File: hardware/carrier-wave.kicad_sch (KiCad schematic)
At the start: 22 parts, among them J1 USB C 2.0, U1 STM32G0B1CBTx, U2 OPA695, U3 THS3491, U4 AD9834, U5 LM27762, U7 TS5A3159ADCK, U8 LM2990SX-12, U9 LM2940S-12

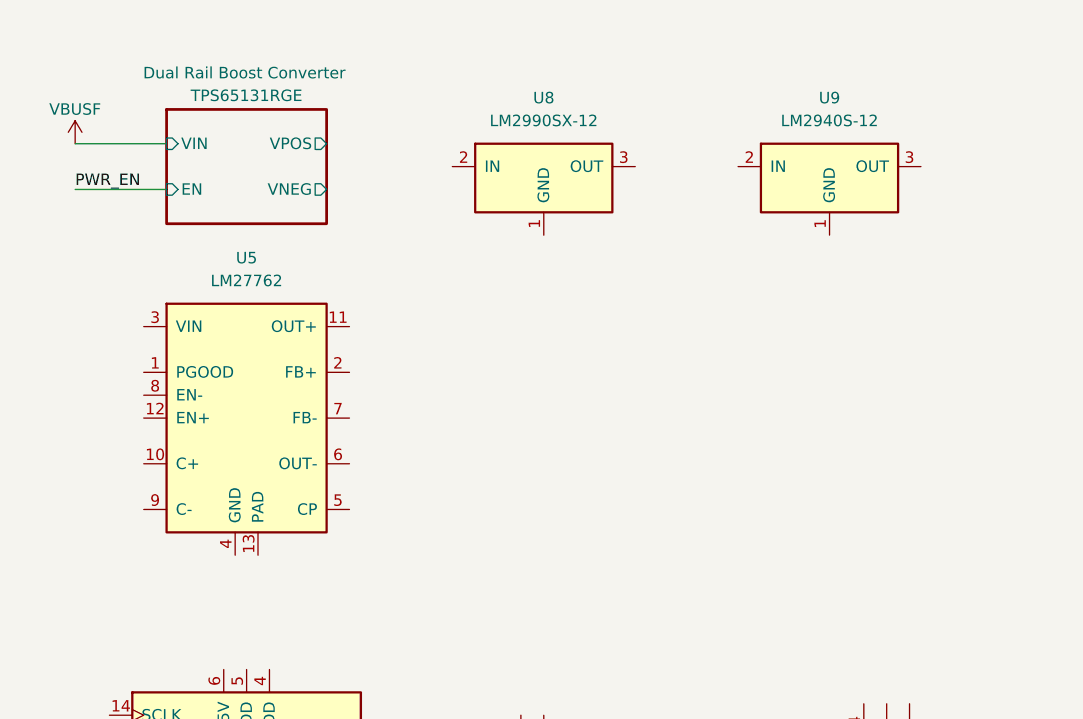
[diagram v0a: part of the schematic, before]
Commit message: Complete 12V rail supply
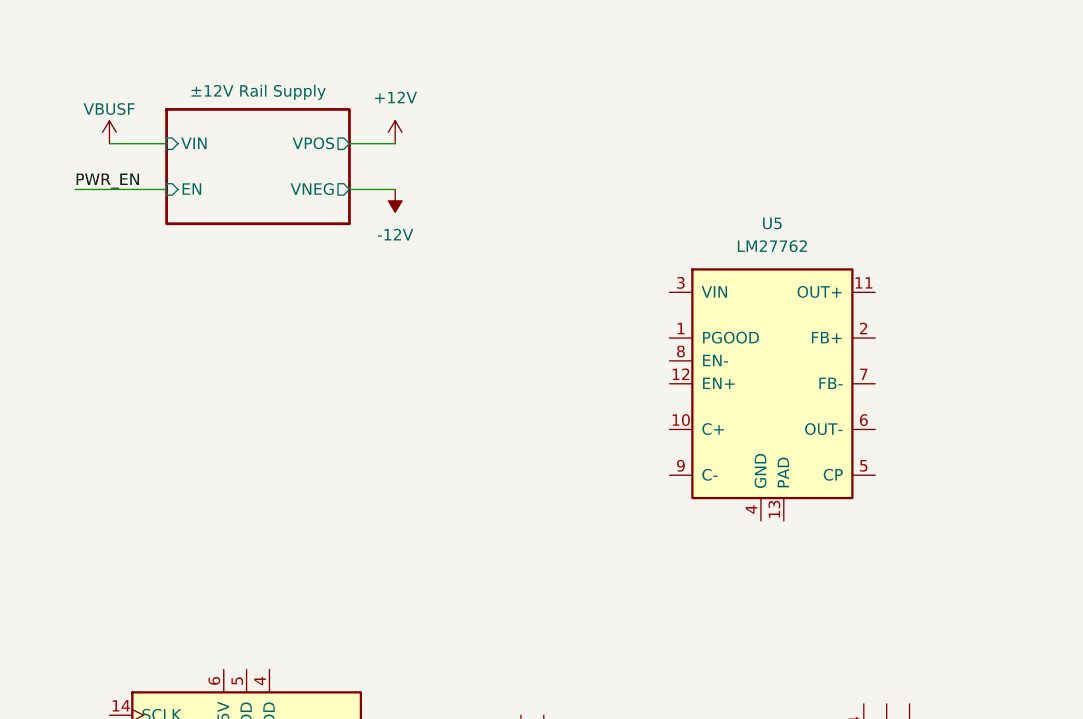
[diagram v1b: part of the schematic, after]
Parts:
- removed U8: LM2990SX-12, Package_TO_SOT_SMD:TO-263-3_TabPin2, symbol Regulator_Linear:LM2990SX-12
- removed U9: LM2940S-12, Package_TO_SOT_SMD:TO-263-3_TabPin2, symbol Regulator_Linear:LM2990SX-12
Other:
- sheet Dual Rail Boost Converter renamed ±12V Rail Supply
- sheet ±12V Rail Supply: file boost_coverter.kicad_sch -> 12V_boost_converter.kicad_sch
- moved on the sheet: U5
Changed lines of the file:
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@@
 	(wire
 		(pts
+			(xy 50.8 27.94) (xy 55.88 27.94)
+		)
+		(stroke
+			(width 0)
+			(type default)
+		)
+	)
+	(wire
+		(pts
 			(xy 182.88 151.13) (xy 182.88 149.86)
 		)
@@
 	(wire
 		(pts
+			(xy 50.8 33.02) (xy 55.88 33.02)
+		)
+		(stroke
+			(width 0)
+			(type default)
+		)
+	)
+	(wire
+		(pts
 			(xy 222.25 160.02) (xy 222.25 161.29)
 		)
@@
 	(wire
 		(pts
-			(xy 20.32 27.94) (xy 30.48 27.94)
+			(xy 24.13 27.94) (xy 30.48 27.94)
 		)
 		(stroke
@@
 	(symbol
 		(lib_id "power:VBUS")
-		(at 20.32 27.94 0)
+		(at 24.13 27.94 0)
 		(unit 1)
 		(body_style 1)
@@
 		(dnp no)
 		(property "Reference" "#PWR06"
-			(at 20.32 31.75 0)
+			(at 24.13 31.75 0)
 			(hide yes)
 			(show_name no)
@@
 		)
 		(property "Value" "VBUSF"
-			(at 20.32 24.13 0)
+			(at 24.13 24.13 0)
 			(show_name no)
 			(do_not_autoplace no)
@@
 		)
 		(property "Footprint" ""
-			(at 20.32 27.94 0)
+			(at 24.13 27.94 0)
 			(hide yes)
 			(show_name no)
@@
 		)
 		(property "Datasheet" ""
-			(at 20.32 27.94 0)
+			(at 24.13 27.94 0)
 			(hide yes)
 			(show_name no)
@@
 		)
 		(property "Description" "Power symbol creates a global label with name \"VBUS\""
-			(at 20.32 27.94 0)
+			(at 24.13 27.94 0)
 			(hide yes)
 			(show_name no)
@@
 	)
 	(symbol
-		(lib_id "Regulator_Linear:LM2990SX-12")
-		(at 72.39 30.48 0)
+		(lib_id "power:-12V")
+		(at 55.88 33.02 0)
+		(mirror x)
 		(unit 1)
 		(body_style 1)
@@
 		(dnp no)
 		(fields_autoplaced yes)
-		(property "Reference" "U8"
-			(at 72.39 22.86 0)
+		(property "Reference" "#PWR0108"
+			(at 55.88 29.21 0)
+			(hide yes)
 			(show_name no)
 			(do_not_autoplace no)
@@
 			)
 		)
-		(property "Value" "LM2990SX-12"
-			(at 72.39 25.4 0)
+		(property "Value" "-12V"
+			(at 55.88 38.1 0)
 			(show_name no)
 			(do_not_autoplace no)
@@
 			)
 		)
-		(property "Footprint" "Package_TO_SOT_SMD:TO-263-3_TabPin2"
-			(at 72.39 40.64 0)
+		(property "Footprint" ""
+			(at 55.88 33.02 0)
 			(hide yes)
 			(show_name no)
@@
 			)
 		)
-		(property "Datasheet" "http://www.ti.com/lit/ds/symlink/lm2990.pdf"
-			(at 40.64 11.43 0)
+		(property "Datasheet" ""
+			(at 55.88 33.02 0)
 			(hide yes)
 			(show_name no)
@@
 			)
 		)
-		(property "Description" "Three termianl low-dropout 1A negative voltage regulator, Input -6V to -26V, Out -12V"
-			(at 72.39 30.48 0)
+		(property "Description" "Power symbol creates a global label with name \"-12V\""
+			(at 55.88 33.02 0)
 			(hide yes)
 			(show_name no)
@@
 			)
 		)
-		(pin "2"
-		)
 		(pin "1"
 		)
-		(pin "3"
-		)
 		(instances
 			(project "carrier-wave"
 				(path "/dc900721-a2e3-4f11-b4f2-59bb3a47422e"
-					(reference "U8")
+					(reference "#PWR0108")
 					(unit 1)
 				)
@@
 	(symbol
 		(lib_id "Regulator_SwitchedCapacitor:LM27762")
-		(at 38.1 53.34 0)
+		(at 96.52 49.53 0)
 		(unit 1)
 		(body_style 1)
@@
 		(fields_autoplaced yes)
 		(property "Reference" "U5"
-			(at 39.37 40.64 0)
+			(at 97.79 36.83 0)
 			(show_name no)
 			(do_not_autoplace no)
@@
 		)
 		(property "Value" "LM27762"
-			(at 39.37 43.18 0)
+			(at 97.79 39.37 0)
 			(show_name no)
 			(do_not_autoplace no)
@@
 		)
 		(property "Footprint" "Package_SON:WSON-12-1EP_3x2mm_P0.5mm_EP1x2.65_ThermalVias"
-			(at 41.91 72.39 0)
+			(at 100.33 68.58 0)
 			(hide yes)
 			(show_name no)
@@
 		)
 		(property "Datasheet" "http://www.ti.com/lit/ds/symlink/lm27762.pdf"
-			(at 101.6 63.5 0)
+			(at 160.02 59.69 0)
 			(hide yes)
 			(show_name no)
@@
 		)
 		(property "Description" "Low-noise inverting charge pump with both positive and negative LDO's, with 2.7V-5.5V input to +1.5 to +5V and -1.5 to -5V Output Voltage, WSON-12"
-			(at 38.1 53.34 0)
+			(at 96.52 49.53 0)
 			(hide yes)
 			(show_name no)
@@
 	)
 	(symbol
-		(lib_id "Regulator_Linear:LM2990SX-12")
-		(at 104.14 30.48 0)
-		(unit 1)
-		(body_style 1)
-		(exclude_from_sim no)
-		(in_bom yes)
-		(on_board yes)
-		(in_pos_files yes)
-		(dnp no)
-		(fields_autoplaced yes)
-		(property "Reference" "U9"
-			(at 104.14 22.86 0)
-			(show_name no)
-			(do_not_autoplace no)
-			(effects
-				(font
-					(size 1.27 1.27)
-				)
-			)
-		)
-		(property "Value" "LM2940S-12"
-			(at 104.14 25.4 0)
-			(show_name no)
-			(do_not_autoplace no)
-			(effects
-				(font
-					(size 1.27 1.27)
-				)
-			)
-		)
-		(property "Footprint" "Package_TO_SOT_SMD:TO-263-3_TabPin2"
-			(at 104.14 40.64 0)
-			(hide yes)
-			(show_name no)
-			(do_not_autoplace no)
-			(effects
-				(font
-					(size 1.27 1.27)
-				)
-			)
-		)
-		(property "Datasheet" "https://www.ti.com/general/docs/suppproductinfo.tsp?distId=10&gotoUrl=https%3A%2F%2Fwww.ti.com%2Flit%2Fgpn%2Flm2940-n"
-			(at 72.39 11.43 0)
-			(hide yes)
-			(show_name no)
-			(do_not_autoplace no)
-			(effects
-				(font
-					(size 1.27 1.27)
-				)
-			)
-		)
-		(property "Description" "Three termianl low-dropout 1A positive voltage regulator, Input 6V to 26V, Out 12V"
-			(at 104.14 30.48 0)
-			(hide yes)
-			(show_name no)
-			(do_not_autoplace no)
-			(effects
-				(font
-					(size 1.27 1.27)
-				)
-			)
-		)
-		(pin "2"
-		)
-		(pin "1"
-		)
-		(pin "3"
-		)
-		(instances
-			(project "carrier-wave"
-				(path "/dc900721-a2e3-4f11-b4f2-59bb3a47422e"
-					(reference "U9")
-					(unit 1)
-				)
-			)
-		)
-	)
-	(symbol
 		(lib_id "Regulator_Linear:AP2112K-3.3")
 		(at 201.93 153.67 0)
@@
 	)
 	(symbol
+		(lib_id "power:+12V")
+		(at 55.88 27.94 0)
+		(unit 1)
+		(body_style 1)
+		(exclude_from_sim no)
+		(in_bom yes)
+		(on_board yes)
+		(in_pos_files yes)
+		(dnp no)
+		(fields_autoplaced yes)
+		(property "Reference" "#PWR0107"
+			(at 55.88 31.75 0)
+			(hide yes)
+			(show_name no)
+			(do_not_autoplace no)
+			(effects
+				(font
+					(size 1.27 1.27)
+				)
+			)
+		)
+		(property "Value" "+12V"
+			(at 55.88 22.86 0)
+			(show_name no)
+			(do_not_autoplace no)
+			(effects
+				(font
+					(size 1.27 1.27)
+				)
+			)
+		)
+		(property "Footprint" ""
+			(at 55.88 27.94 0)
+			(hide yes)
+			(show_name no)
+			(do_not_autoplace no)
+			(effects
+				(font
+					(size 1.27 1.27)
+				)
+			)
+		)
+		(property "Datasheet" ""
+			(at 55.88 27.94 0)
+			(hide yes)
+			(show_name no)
+			(do_not_autoplace no)
+			(effects
+				(font
+					(size 1.27 1.27)
+				)
+			)
+		)
+		(property "Description" "Power symbol creates a global label with name \"+12V\""
+			(at 55.88 27.94 0)
+			(hide yes)
+			(show_name no)
+			(do_not_autoplace no)
+			(effects
+				(font
+					(size 1.27 1.27)
+				)
+			)
+		)
+		(pin "1"
+		)
+		(instances
+			(project "carrier-wave"
+				(path "/dc900721-a2e3-4f11-b4f2-59bb3a47422e"
+					(reference "#PWR0107")
+					(unit 1)
+				)
+			)
+		)
+	)
+	(symbol
 		(lib_id "Amplifier_Operational:THS3491xDDA")
 		(at 110.49 97.79 0)
@@
 	(sheet
 		(at 30.48 24.13)
-		(size 17.78 12.7)
+		(size 20.32 12.7)
 		(exclude_from_sim no)
 		(in_bom yes)
@@
 			(color 255 229 191 1)
 		)
-		(property "Sheetname" "Dual Rail Boost Converter"
-			(at 39.116 20.828 0)
+		(property "Sheetname" "±12V Rail Supply"
+			(at 40.64 22.86 0)
 			(show_name no)
 			(do_not_autoplace no)
@@
 			)
 		)
-		(property "Sheetfile" "boost_coverter.kicad_sch"
+		(property "Sheetfile" "12V_boost_converter.kicad_sch"
 			(at 30.48 37.4146 0)
 			(hide yes)
@@
 			)
 		)
-		(property "Component" "TPS65131RGE"
-			(at 39.37 22.606 0)
+		(property "Component" "TPS65131RGE / LM2940 & LM2990"
+			(at 48.26 22.86 0)
+			(hide yes)
 			(show_name no)
 			(do_not_autoplace no)
@@
 		)
 		(pin "VNEG" output
-			(at 48.26 33.02 0)
+			(at 50.8 33.02 0)
 			(effects
 				(font
@@
 		)
 		(pin "VPOS" output
-			(at 48.26 27.94 0)
+			(at 50.8 27.94 0)
 			(effects
 				(font

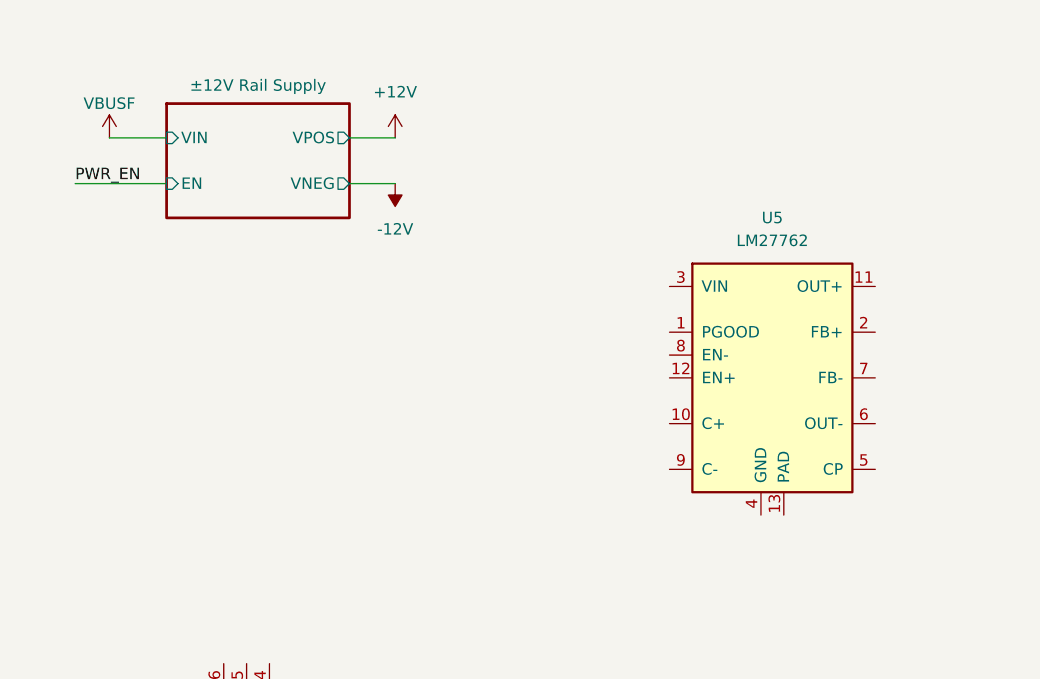
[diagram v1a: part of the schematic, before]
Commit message: Begin charge pump schematic
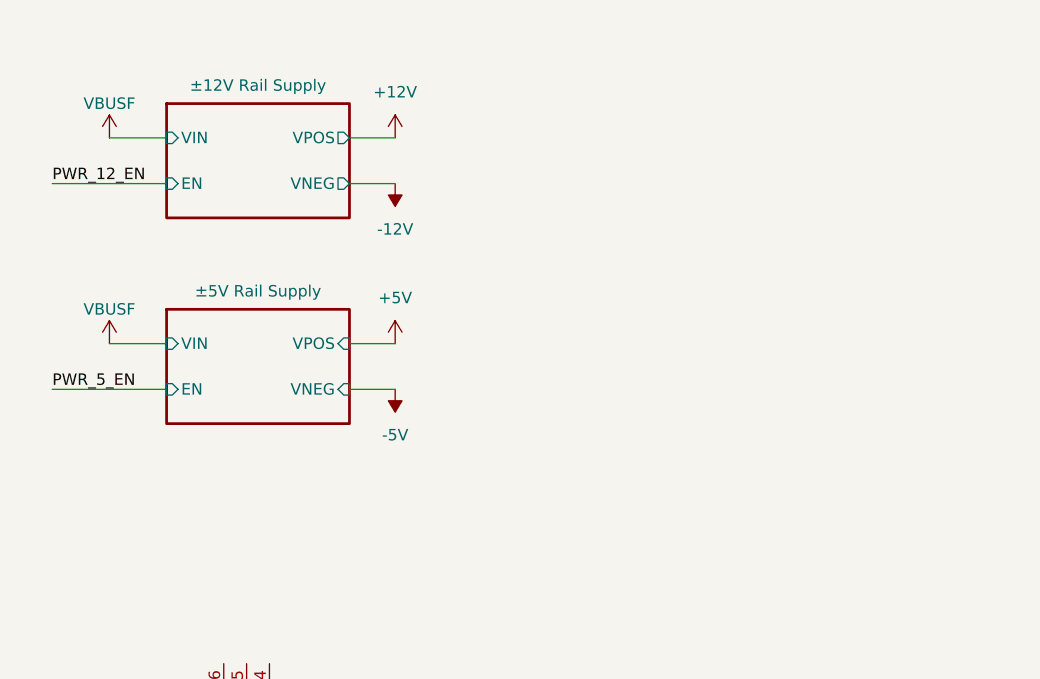
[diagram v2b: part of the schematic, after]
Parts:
- removed U5: LM27762, Package_SON:WSON-12-1EP_3x2mm_P0.5mm_EP1x2.65_ThermalVias, symbol Regulator_SwitchedCapacitor:LM27762
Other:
- added sheet ±5V Rail Supply (charge_pump_ldo.kicad_sch)

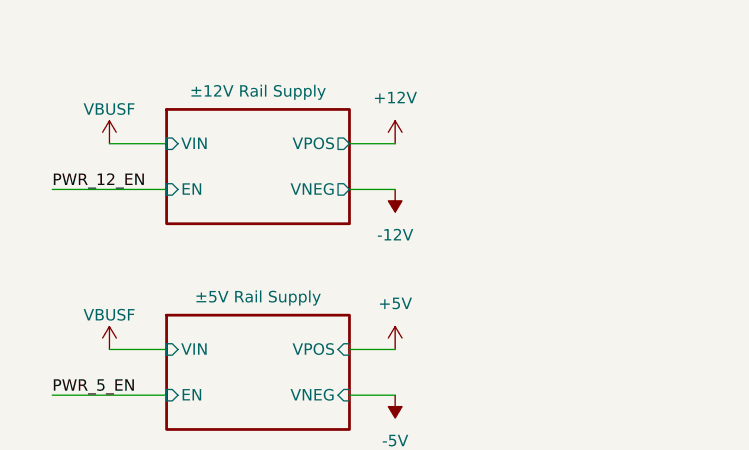
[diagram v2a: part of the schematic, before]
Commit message: Implement TPS7A39 and Annotate
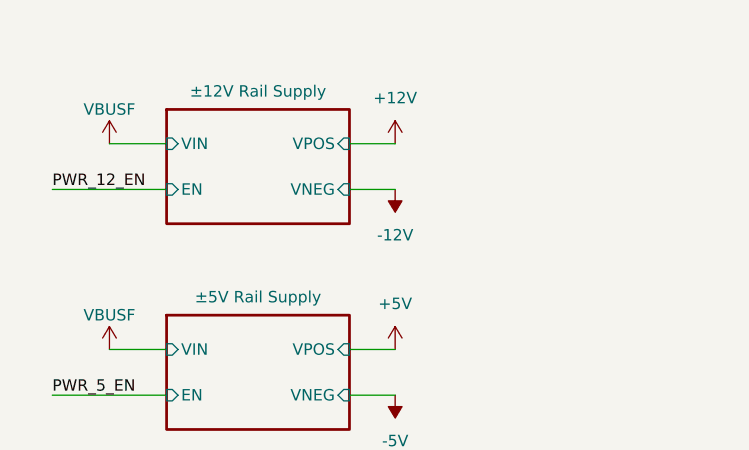
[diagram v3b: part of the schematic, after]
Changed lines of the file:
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@@
 			)
 		)
-		(pin "VNEG" output
+		(pin "VNEG" input
 			(at 50.8 33.02 0)
 			(effects
@@
 			)
 		)
-		(pin "VPOS" output
+		(pin "VPOS" input
 			(at 50.8 27.94 0)
 			(effects
